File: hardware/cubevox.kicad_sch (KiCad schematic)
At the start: 150 parts, among them J101 J_IN NCJ6FA-H, J106 DC 9V, J108 OUT 6.35mm, J117 OLED SH1106, K101 G6K-2F-Y DC5, K102 G6K-2F-Y DC5, Q101 MMBT3904, SW101 ST-0-102 bat toggle, SW102 ST-0-102 bat toggle, SW103 ST-0-102 bat toggle, SW104 ST-0-102 bat toggle, SW105 ST-0-102 bat toggle, SW106 ST-0-102 bat toggle, SW107 ST-0-102 bat toggle, SW108 ST-0-102 bat toggle, U101 CD74HC4067, U103 AP63205WU-7, U104 OPA2197IDR, U105 OPA2197IDR, U106 OPA2197IDR

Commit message: feat(sch): split VREF buffer east, local 5VA_W/BIAS_W for output stage
The VREF follower moves to a new single op-amp U108 (OPA197IDBVR, C221351) with its own 100 nF (C167), so VREF no longer leaves the east side. U106 stays at the west output stage: its A half becomes a tied-off follower (pins 1-2 on U106A_OUT, pin 3 on BIAS_W). The output stage gets a local supply 5VA_W (FB102 from 5V, C168 10 uF, C130 kept at pin 8) and a local bias BIAS_W (R154/R155 10 k divider, C169 10 uF); R123 biases DAC_ATT to BIAS_W. ERC: no new violations.
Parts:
- added C167: 100nF, Capacitor_SMD:C_0402_1005Metric, symbol Device:C
- added C168, C169: 10uF, Capacitor_SMD:C_0805_2012Metric, symbol Device:C
- added FB102: 120R@100MHz, Inductor_SMD:L_0603_1608Metric, symbol Device:FerriteBead
- added R154, R155: 10k, Resistor_SMD:R_0402_1005Metric, symbol Device:R
- added U108: OPA197IDBVR, Package_TO_SOT_SMD:SOT-23-5, symbol cubevox:OPA197IDBVR
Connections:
- net 5V: now also FB102.1
- net 5VA: now also C167.1, U108.5 (V+); no longer C130.1, U106.8 (+VS)
- net GND: now also C167.2, C168.2, C169.2, R155.2, U108.2 (V-)
- net VREF: no longer R123.2
- net VREF_BUF: now also U108.1 (OUT), U108.4 (-IN); no longer U106.1 (OUT/A), U106.2 (-IN/A)
- net VREF_DIV: now also U108.3 (+IN); no longer U106.3 (+IN/A)
- new net 5VA_W: C130.1, C168.1, FB102.2, R154.1, U106.8 (+VS)
- new net BIAS_W: C169.1, R123.2, R154.2, R155.1, U106.3 (+IN/A)
- new net U106A_OUT: U106.1 (OUT/A), U106.2 (-IN/A)

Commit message: feat(hardware): J117 OLED header becomes hanxia 5 mm SMD socket C42379197 (D0352)
JLC's hand-inserted through-hole headers came out crooked on the previous board. An SMD socket is machine-placed and self-centres in reflow. Library footprint, schematic LCSC fields, spec item 22 and PARTS.md follow the board.
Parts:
- J117: LCSC owner-supplied module, hand-plugged -> C42379197
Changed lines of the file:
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@@
 			)
 		)
-		(property "LCSC" "owner-supplied module, hand-plugged"
+		(property "LCSC" "C42379197"
 			(at 797.56 596.9 0)
 			(hide yes)

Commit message: feat(sch): slots revision, KEY/SEMITONES pots, bypass relay out, MUTE_SW
ENC102/ENC103 and their debounce RC (R130-R133, C146-C149) become pots
RV115/RV116 on U101 I14/I15 (POT15/POT16). K101, D104 and the PRE_OUT dry
path leave, DAC_ATT joins BUF_IN. SWBYPASS1 now drives MUTE_SW (the former
FX_ON_SENSE); PB7, PB8, PB9, PE0 are no-connect. ERC: 0 errors.
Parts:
- removed C146, C147, C148, C149: 100nF, cubevox:C0603, symbol Device:C
- removed D104: 1N4148W, cubevox:SOD-123F_L2.7-W1.6-LS3.8-RD, symbol cubevox:1N4148W_C81598
- removed ENC102, ENC103: EC11E15204A3, cubevox:SW-TH_EC11E, symbol cubevox:EC11E15204A3
- removed K101: G6K-2F-Y DC5, cubevox:RELAY-SMD_G6K-2F-X-XX, symbol cubevox:G6K-2F-Y-DC5
- removed R130, R131, R132, R133: 10k, cubevox:R0603, symbol Device:R
- added RV115, RV116: 10k, cubevox:RES-ADJ-TH_RK09D1130C2P, symbol cubevox:RK09D1130C2P
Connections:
- net DAC_ATT is gone; now on net BUF_IN: R122.2, R123.1
- net SW_BYPASS is gone; now on net MUTE_SW: SWBYPASS1.2 (COM)
- net 3V3A: now also RV115.3, RV116.3
- net 5V: no longer SWBYPASS1.1 (T1)
- net GND: now also SWBYPASS1.1 (T1), RV115.1, RV116.1; no longer U101.16 (I15), U101.17 (I14)
- net FX_ON_SENSE renamed MUTE_SW
- new net POT15: RV115.2, U101.17 (I14)
- new net POT16: RV116.2, U101.16 (I15)
- no-connect marks 55 -> 54
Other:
- sheet h7core_block ports: added MUTE_SW; removed ENC_KEY_A, ENC_KEY_B, ENC_SEMI_A, ENC_SEMI_B, FX_ON_SENSE
- note added: "16 pots to U101 (the mux is full), 1 encoder, 8 toggles, OLED header"
- note added: "470R / 2.2nF filter, 10uF, BUF_IN = 0.6 x DAC about VREF"
- note added: "5. MUTE TOGGLE"
- note added: "MUTE_SW low = muted. K102 (section 8) does the muting"
- note added: "Mute toggle. Common to MUTE_SW, one throw to GND, other throw open"
- note removed: "14 pots to U101 (C14, C15 on GND), 3 encoders, 8 toggles, OLED header"
- note removed: "470R / 2.2nF filter, 10uF, DAC_ATT = 0.6 x DAC about VREF"
- note removed: "5. BYPASS"
- note removed: "Bypass toggle. Common to the coil, one throw to 5V"
- note removed: "Pole A COM BUF_IN, NC PRE_OUT, NO DAC_ATT. Pole B COM GND, NO FX_ON_SENSE (low = effect on). Coil on = effect on"

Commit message: feat(sch): re-map U101 west channels to the pot row order
The west POT rows' order down the band is fixed by their drops, and the vias' x order by U101's pin order; the two disagreed, so verticals stepped across each other's rows. POT09-15 now sit on I8-I14 so that pin order equals row order. Firmware slots.cpp follows, so every knob still reads the same parameter; PINMAP carries the channel table.
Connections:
- net POT09: now also U101.18 (I13); no longer U101.23 (I8)
- net POT10: now also U101.17 (I14); no longer U101.22 (I9)
- net POT11: now also U101.22 (I9); no longer U101.21 (I10)
- net POT13: now also U101.23 (I8); no longer U101.19 (I12)
- net POT14: now also U101.21 (I10); no longer U101.18 (I13)
- net POT15: now also U101.19 (I12); no longer U101.17 (I14)
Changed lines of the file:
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@@
 	)
 	(label "POT15"
-		(at 213.36 435.61 0)
+		(at 213.36 430.53 0)
 		(fields_autoplaced yes)
 		(effects
@@
 	)
 	(label "POT14"
-		(at 213.36 433.07 0)
+		(at 213.36 425.45 0)
 		(fields_autoplaced yes)
 		(effects
@@
 	)
 	(label "POT13"
-		(at 213.36 430.53 0)
+		(at 213.36 420.37 0)
 		(fields_autoplaced yes)
 		(effects
@@
 	)
 	(label "POT11"
-		(at 213.36 425.45 0)
+		(at 213.36 422.91 0)
 		(fields_autoplaced yes)
 		(effects
@@
 	)
 	(label "POT10"
-		(at 213.36 422.91 0)
+		(at 213.36 435.61 0)
 		(fields_autoplaced yes)
 		(effects
@@
 	)
 	(label "POT09"
-		(at 213.36 420.37 0)
+		(at 213.36 433.07 0)
 		(fields_autoplaced yes)
 		(effects

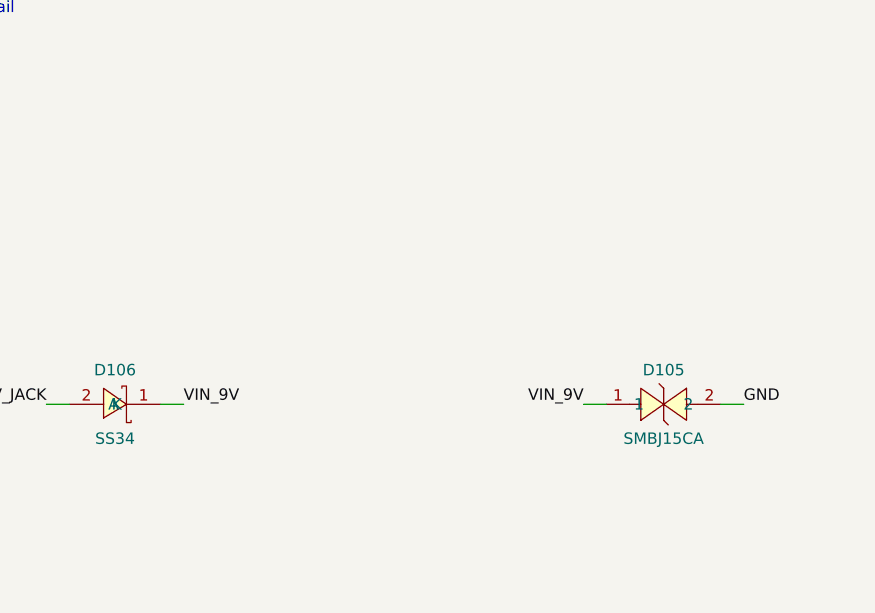
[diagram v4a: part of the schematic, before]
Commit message: feat(sch): pre-fab parts, log gain pot, test points, R7 68k
SMBJ20CA for D105, R158 100k pull-up on LDO_EN, C170 10uF at U6, R7 68k, RVGAIN1 RK09D117000C (15A), TP1-TP5. Per docs/reference/PREFAB_REVIEW_2026-10-08.md.
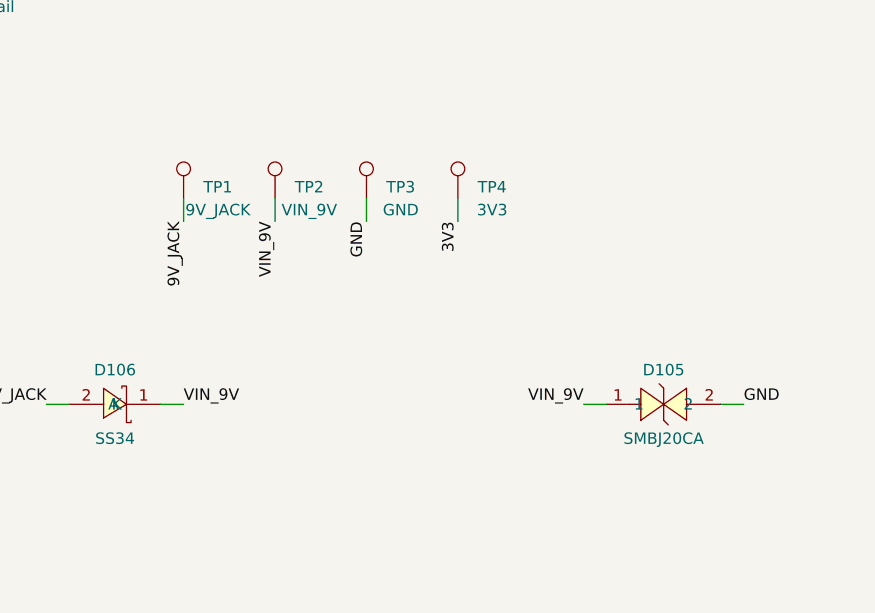
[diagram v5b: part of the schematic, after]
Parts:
- added TP1: 9V_JACK, TestPoint:TestPoint_Pad_D1.5mm, symbol Connector:TestPoint
- added TP2: VIN_9V, TestPoint:TestPoint_Pad_D1.5mm, symbol Connector:TestPoint
- added TP3: GND, TestPoint:TestPoint_Pad_D1.5mm, symbol Connector:TestPoint
- added TP4: 3V3, TestPoint:TestPoint_Pad_D1.5mm, symbol Connector:TestPoint
- D105: value SMBJ15CA -> SMBJ20CA; LCSC C19077570 -> C113992; MPN SMBJ15CA -> SMBJ20CA
- RVGAIN1: LCSC C361173 -> C470307; MPN RK09D1130C2P -> RK09D117000C; Note (none) -> 15A log taper, 30 mm shaft
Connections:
- net 3V3: now also TP4.1
- net 9V_JACK: now also TP1.1
- net GND: now also TP3.1
- net VIN_9V: now also TP2.1

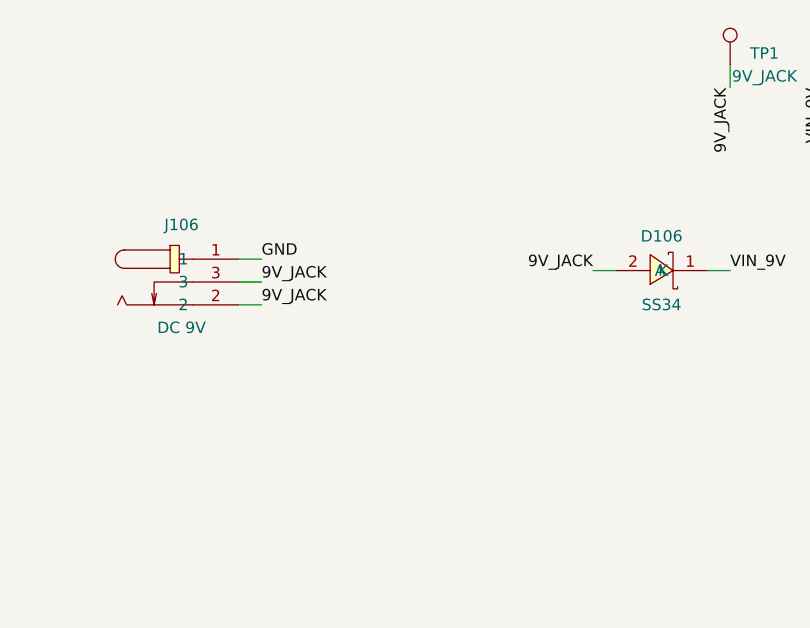
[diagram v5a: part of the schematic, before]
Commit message: feat(hardware): power switch SWPWR1 on the 9 V input, J101 west to x 175
SS-12D11-G050 slide switch (C17179528) in series between the barrel jack
and the SS34, owner-soldered on B.Cu between J101 and J106, out of the JLC
BOM and CPL. J106 pins now carry 9V_PLUG; the switch returns 9V_JACK. The
EasyEDA STEP has its origin at the body centre, so the model carries a
measured offset. Owner routed the nine open connections; gates ALL PASS.
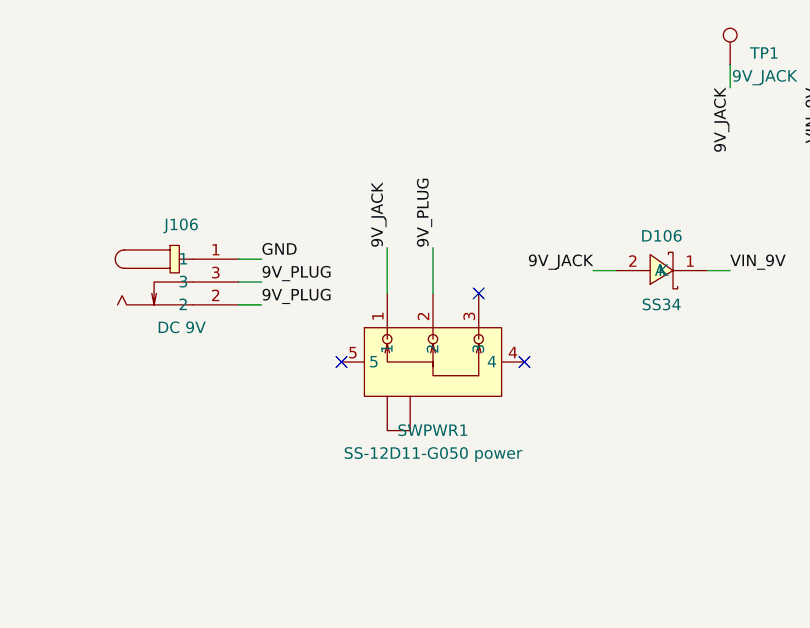
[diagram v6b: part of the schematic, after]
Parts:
- added SWPWR1: SS-12D11-G050 power, cubevox:SW-TH_5P-P4.70_SS-12D11-G050, symbol cubevox:SS-12D11-G050
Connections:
- net 9V_JACK: now also SWPWR1.1; no longer J106.2, J106.3
- new net 9V_PLUG: J106.2, J106.3, SWPWR1.2
- no-connect marks 54 -> 57
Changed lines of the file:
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@@
 		)
 	)
-	(label "9V_JACK"
+	(label "9V_PLUG"
 		(at 158.75 82.55 0)
 		(fields_autoplaced yes)
@@
 		)
 	)
-	(label "9V_JACK"
+	(label "9V_PLUG"
 		(at 158.75 80.01 0)
 		(fields_autoplaced yes)
@@
 	)
 	(symbol
+		(lib_id "cubevox:SS-12D11-G050")
+		(at 177.8 88.9 0)
+		(unit 1)
+		(exclude_from_sim no)
+		(in_bom no)
+		(on_board yes)
+		(in_pos_files no)
+		(dnp no)
+		(property "Reference" "SWPWR1"
+			(at 177.8 96.52000000000001 0)
+			(effects
+				(font
+					(size 1.27 1.27)
+				)
+			)
+		)
+		(property "Value" "SS-12D11-G050 power"
+			(at 177.8 99.06 0)
+			(effects
+				(font
+					(size 1.27 1.27)
+				)
+			)
+		)
+		(property "Footprint" "cubevox:SW-TH_5P-P4.70_SS-12D11-G050"
+			(at 177.8 88.9 0)
+			(hide yes)
+			(effects
+				(font
+					(size 1.27 1.27)
+				)
+			)
+		)
+		(property "Datasheet" "https://www.lcsc.com/datasheet/C17179528.pdf"
+			(at 177.8 88.9 0)
+			(hide yes)
+			(effects
+				(font
+					(size 1.27 1.27)
+				)
+			)
+		)
+		(property "LCSC" "C17179528"
+			(at 177.8 88.9 0)
+			(hide yes)
+			(effects
+				(font
+					(size 1.27 1.27)
+				)
+			)
+		)
+		(property "MPN" "SS-12D11-G050"
+			(at 177.8 88.9 0)
+			(hide yes)
+			(effects
+				(font
+					(size 1.27 1.27)
+				)
+			)
+		)
+		(pin "1"
+		)
+		(pin "2"
+		)
+		(pin "3"
+		)
+		(pin "4"
+		)
+		(pin "5"
+		)
+		(instances
+			(project "cubevox"
+				(path "/99ad1494-2bf8-5051-8886-2c8b83c86254"
+					(reference "SWPWR1")
+					(unit 1)
+				)
+			)
+		)
+	)
+	(wire
+		(pts
+			(xy 172.72 81.28) (xy 172.72 76.2)
+		)
+		(stroke
+			(width 0)
+			(type default)
+		)
+	)
+	(label "9V_JACK"
+		(at 172.72 76.2 90)
+		(fields_autoplaced yes)
+		(effects
+			(font
+				(size 1.27 1.27)
+			)
+			(justify left bottom)
+		)
+	)
+	(wire
+		(pts
+			(xy 177.8 81.28) (xy 177.8 76.2)
+		)
+		(stroke
+			(width 0)
+			(type default)
+		)
+	)
+	(label "9V_PLUG"
+		(at 177.8 76.2 90)
+		(fields_autoplaced yes)
+		(effects
+			(font
+				(size 1.27 1.27)
+			)
+			(justify left bottom)
+		)
+	)
+	(no_connect
+		(at 182.88000000000002 81.28)
+	)
+	(no_connect
+		(at 187.96 88.9)
+	)
+	(no_connect
+		(at 167.64000000000001 88.9)
+	)
+	(symbol

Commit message: feat(hardware): 25 mm gain pot with divider law, relay-switched 1/4" pad
RVGAIN1 becomes the RK09D1130C2P (C361173) wired as a divider: pin 3 on
G2_BOT through R116 470R to G2_RG, new R159 1k from G2_INV to G2_RG, so
the gain knob adds 0 to +30 dB on top of the fixed 20 dB and never
attenuates.

K103 (G6K-2F-Y DC5, same part and driver set as the mute relay K102)
shorts the 25.7 dB 1/4" pad resistors R102 and R105 when de-energised,
so the rest state is MIC and the SM58 on an XLR-to-1/4" cable reaches
the preamp without the pad. PAD_EN on U1 PB8 (high = PEDAL) drives Q102
through R160/R161 with D110 across the coil. K103 pin 5 carries LINE_N
and pin 6 IN_N so the N leg routes on one layer next to R105.

Astra agreed relay over analog switch; packet and reply under
docs/audits.
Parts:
- added D110: 1N4148W, cubevox:SOD-123F_L2.7-W1.6-LS3.8-RD, symbol cubevox:1N4148W_C81598
- added K103: G6K-2F-Y DC5, cubevox:RELAY-SMD_G6K-2F-X-XX, symbol cubevox:G6K-2F-Y-DC5
- added Q102: MMBT3904, cubevox:SOT-23-3_L2.9-W1.3-P1.90-LS2.4-BR, symbol cubevox:MMBT3904-C20526
- added R159, R160: 1k, cubevox:R0603, symbol Device:R
- added R161: 100k, cubevox:R0603, symbol Device:R
- R116: value 330R -> 470R; LCSC C23138 -> C23179
- RVGAIN1: LCSC C470307 -> C361173; MPN RK09D117000C -> RK09D1130C2P; Note 15A log taper, 30 mm shaft -> 1B linear, 25 mm shaft, same part as the slot pots; divider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
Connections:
- net 5V: now also D110.1 (K), K103.1
- net G2_INV: now also R159.1; no longer R116.1, RVGAIN1.3
- net G2_RG: now also R159.2
- net GND: now also Q102.2 (E), R161.2
- net IN_N: now also K103.6
- net IN_P: now also K103.4
- net LINE_N: now also K103.5
- net LINE_P: now also K103.3
- new net G2_BOT: R116.1, RVGAIN1.3
- new net PAD_BASE: Q102.1 (B), R160.2, R161.1
- new net PAD_COIL: D110.2 (A), K103.8, Q102.3 (C)
- new net PAD_EN: R160.1
- no-connect marks 57 -> 59
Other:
- sheet h7core_block ports: added PAD_EN; removed none

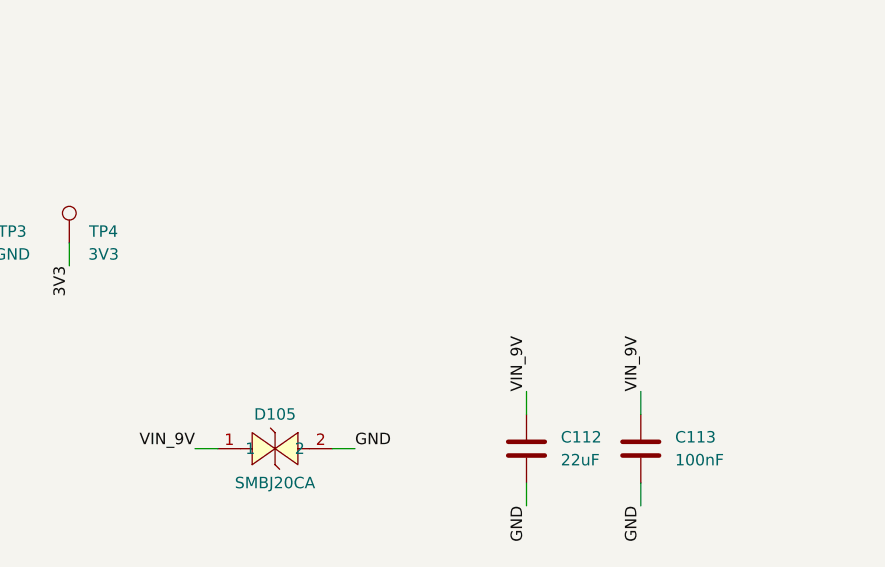
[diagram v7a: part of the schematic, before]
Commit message: feat(hardware): pre-fab audit fixes, pad relay K103 routed, rail test pads
PAD_EN on PE11 (pin 41), K103/D110/Q102/R160/R161/R159 placed and routed.
Audit (docs/audits/2026-10-09-prefab-mega-audit.md, tools/mega_audit.py):
one 3V3 copper loop and two acute off-pad Ts cut, 18 bends at pad or via
edges, 29 off-centre ends, 3 split runs, 8 stair-steps re-laid; 12 parts
moved under 0.5 mm. TP6-TP11 on 3V3A, 5V, 5VA, 5VA_W, VREF_BUF, VDDA with
symbols in both sheets (tools/tp_space.py picks the spots). gates.sh ALL
PASS, ERC 0.
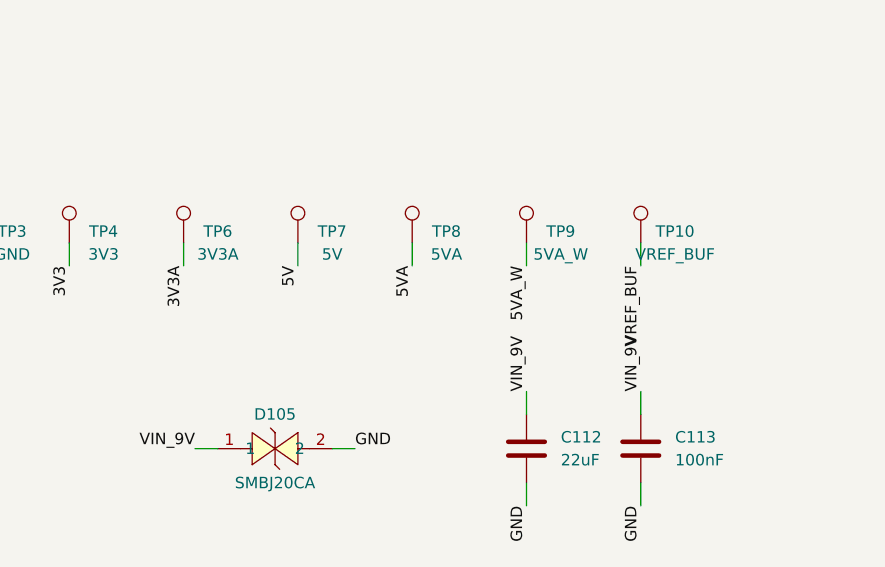
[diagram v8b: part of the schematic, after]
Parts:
- added TP10: VREF_BUF, TestPoint:TestPoint_Pad_D1.5mm, symbol Connector:TestPoint
- added TP6: 3V3A, TestPoint:TestPoint_Pad_D1.5mm, symbol Connector:TestPoint
- added TP7: 5V, TestPoint:TestPoint_Pad_D1.5mm, symbol Connector:TestPoint
- added TP8: 5VA, TestPoint:TestPoint_Pad_D1.5mm, symbol Connector:TestPoint
- added TP9: 5VA_W, TestPoint:TestPoint_Pad_D1.5mm, symbol Connector:TestPoint
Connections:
- net 3V3A: now also TP6.1
- net 5V: now also TP7.1
- net 5VA: now also TP8.1
- net 5VA_W: now also TP9.1
- net VREF_BUF: now also TP10.1
